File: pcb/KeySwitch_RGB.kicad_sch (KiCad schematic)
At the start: 4 parts, among them K19 SW_Push

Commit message: WIP: Updating keyboard matrix to use the new shared part and reorganizing all the LED outputs.
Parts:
- C27: renamed from C17; footprint Capacitor_SMD:C_0805_2012Metric_Pad1.18x1.45mm_HandSolder -> Capacitor_SMD:C_0603_1608Metric_Pad1.08x0.95mm_HandSolder
- K10: renamed from K19; footprint keyswitches:Kailh_socket_MX_optional_reversible -> keyswitches:Kailh_socket_MX_reversible
- renumbered D20 to D19, D21 to D20

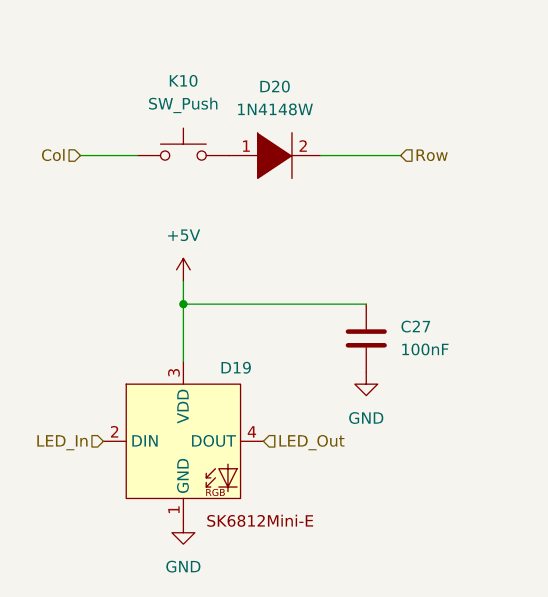
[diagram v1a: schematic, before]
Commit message: Adding reversible MX Sockets and SK6812MiniE footprints, finishing the replacement of Ethernet with a TRRS connector and selectable 0Ohm resistors to swap Rx/Tx for the interconnect.
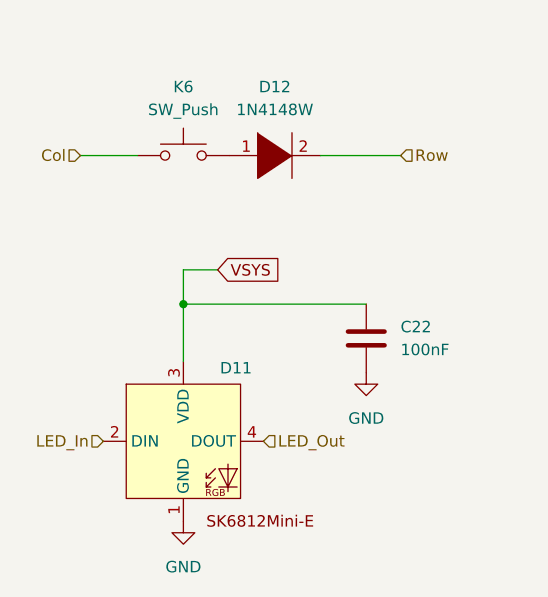
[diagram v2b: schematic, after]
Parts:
- D11: renamed from D19; footprint Extra:SK6812-MINI-E_ReverseMount -> Extra:SK6812-MINI-E_ReverseMount_reversible
- K6: renamed from K10; footprint keyswitches:Kailh_socket_MX_reversible -> Extra:Kailh_socket_MX_reversible
- renumbered C27 to C22, D20 to D12
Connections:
- net +5V renamed VSYS

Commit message: Broke out Underglow LEDs into a common hierarchical sheet for what may be more consistent placements. Additionally created hierarchical PCB layouts and started using the HierarchicalPcb plugin (https://github.com/gauravmm/HierarchicalPcb.git) to automatically layout repeated components for the keymap.
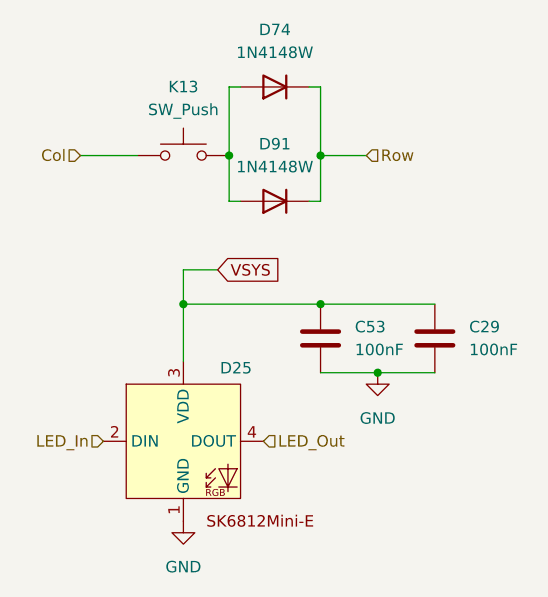
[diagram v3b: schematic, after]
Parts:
- removed D12: 1N4148W, Diode_SMD:D_SOD-123, symbol pspice:DIODE
- added C53: 100nF, Capacitor_SMD:C_0603_1608Metric_Pad1.08x0.95mm_HandSolder, symbol Device:C
- added D74, D91: 1N4148W, Diode_SMD:D_SOD-123, symbol Device:D
- renumbered C22 to C29, D11 to D25, K6 to K13
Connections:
- net GND: now also C53.2
- net Row: now also D74.1 (K), D91.1 (K)
- net VSYS: now also C53.1
- net at K13.2: now also D74.2 (A), D91.2 (A)
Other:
- moved on the sheet: C29

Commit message: Renumbering all reference designations and adding an initial layout for each keyswtich sub-pcb.
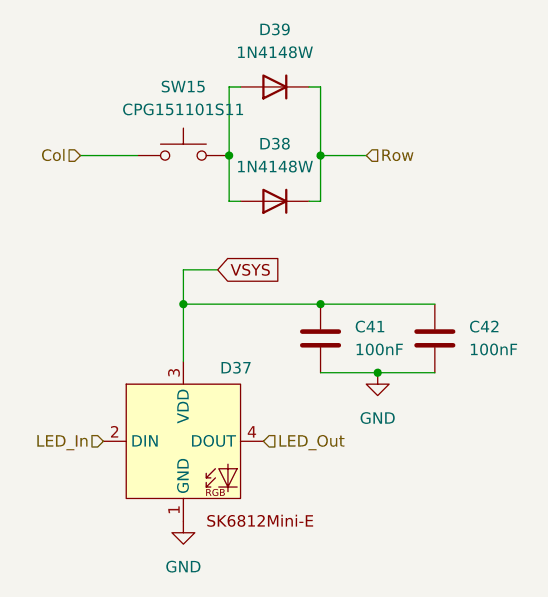
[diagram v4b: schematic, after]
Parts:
- SW15: renamed from K13; value SW_Push -> CPG151101S11
- renumbered C53 to C41, C29 to C42, D25 to D37, D91 to D38, D74 to D39
